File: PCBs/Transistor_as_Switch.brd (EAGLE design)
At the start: 30 x 20 mm, 7 parts, among them T1 2N3904

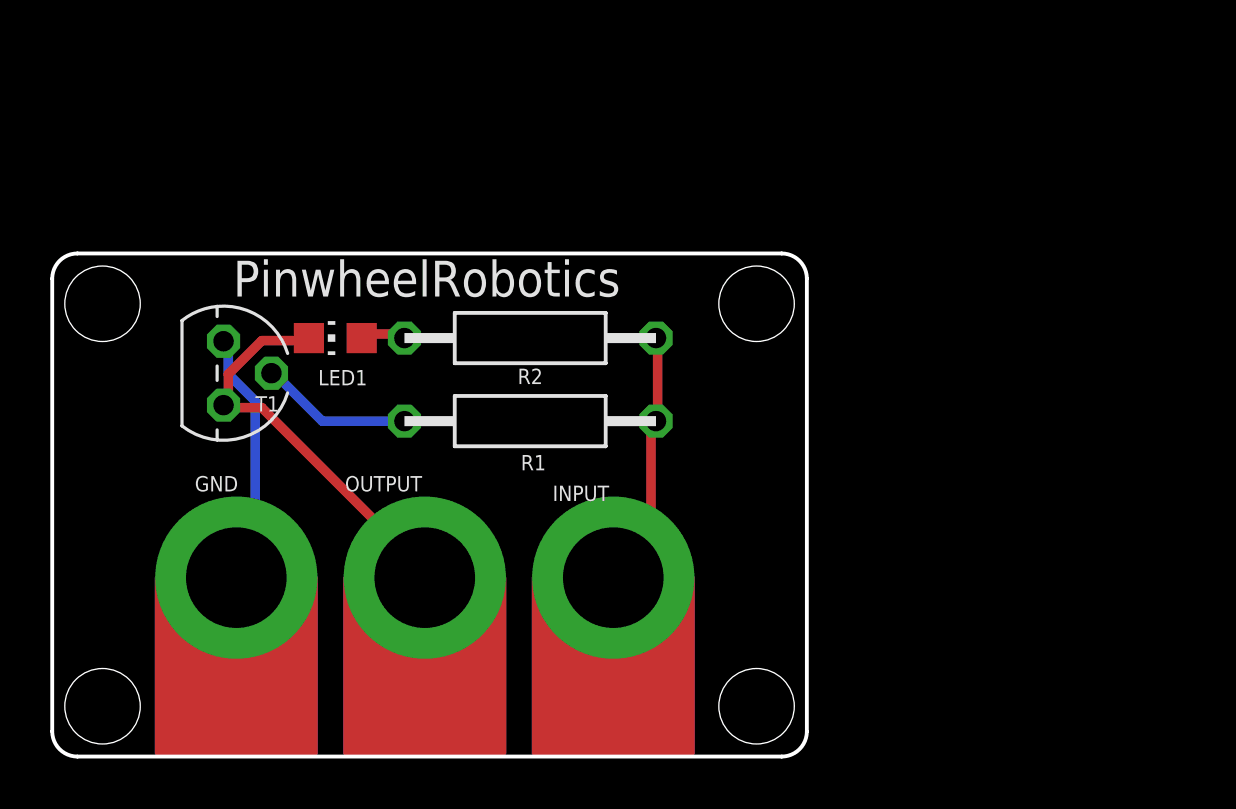
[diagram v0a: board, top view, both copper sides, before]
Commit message: Update for Dim width is 42 length is 28 for type 2 pcb
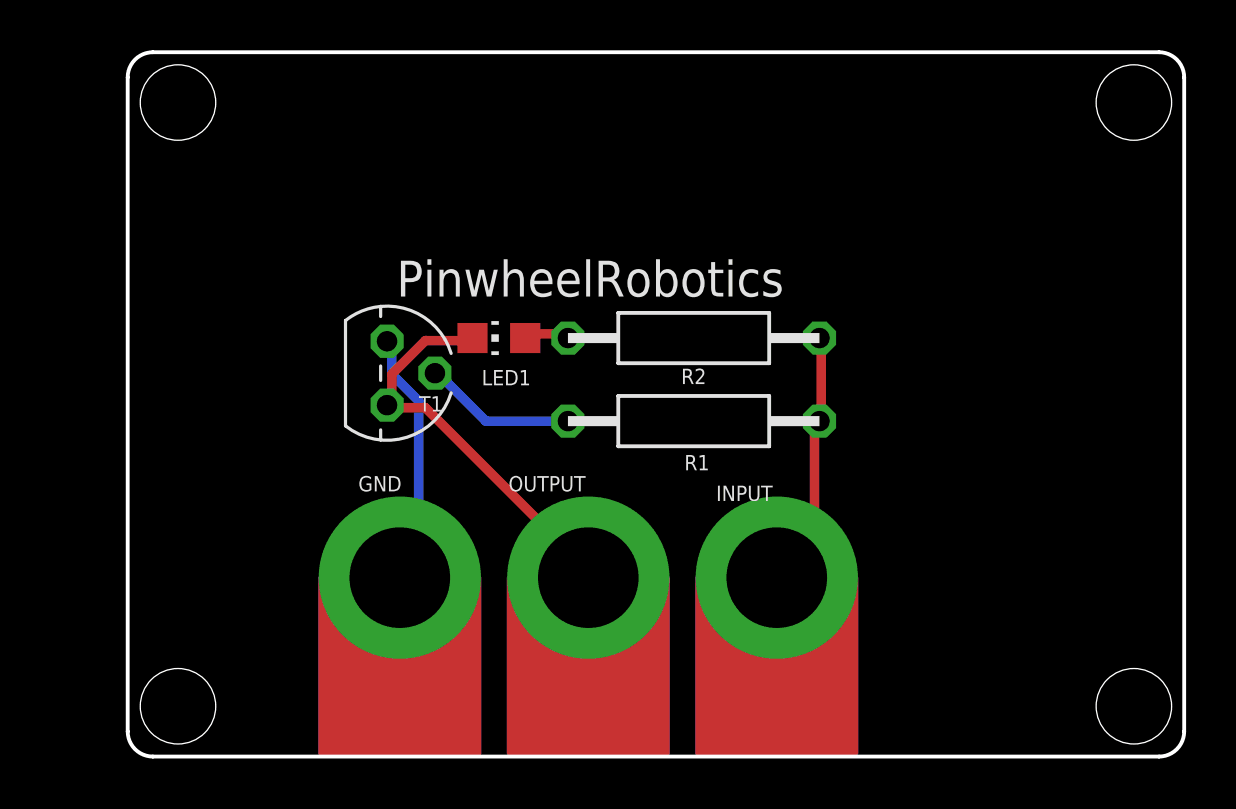
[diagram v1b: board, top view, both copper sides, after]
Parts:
- moved GND 6.50 mm to (10.8, 7.11)
- moved INPUT 6.50 mm to (25.8, 7.11)
- moved LED1 6.50 mm to (14.8, 16.6)
- moved OUTPUT 6.50 mm to (18.3, 7.11)
- moved R1 6.50 mm to (22.5, 13.3)
- moved R2 6.50 mm to (22.5, 16.6)
- moved T1 6.50 mm to (10.3, 15.2)
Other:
- board size 30 x 20 mm -> 42 x 28 mm

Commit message: Corrected hole position for some design , made transistor as switch as category 1
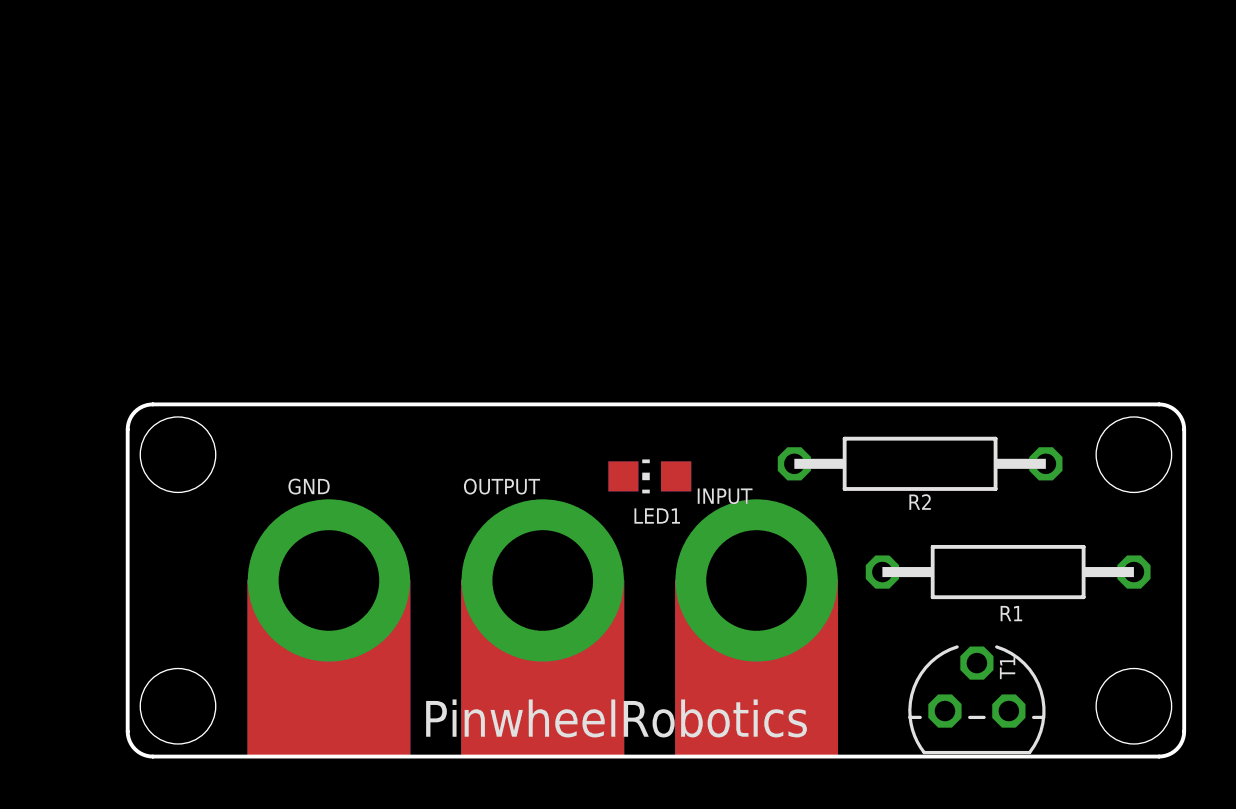
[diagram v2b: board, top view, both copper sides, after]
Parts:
- moved T1 27.0 mm to (33.8, 1.81), turned to 0 degrees
- moved R1 13.9 mm to (35.0, 7.33)
- moved R2 10.3 mm to (31.5, 11.6)
- moved LED1 8.14 mm to (20.8, 11.1)
- moved GND 2.82 mm to (8.00, 7.00)
- moved OUTPUT 1.81 mm to (16.5, 7.00)
- moved INPUT 0.81 mm to (25.0, 7.00)
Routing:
- net N$2: track 16.1 -> 0.00 mm
- net GND: track 10.3 -> 0.00 mm
- net 5V: track 10.5 -> 0.47 mm
- net N$3: track 6.06 -> 0.00 mm
- net N$1: track 1.95 -> 0.00 mm
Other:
- board size 42 x 28 mm -> 42 x 14 mm
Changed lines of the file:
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@@
 <board>
 <plain>
-<wire x1="0" y1="27" x2="0" y2="1" width="0.1524" layer="20"/>
+<wire x1="0" y1="13" x2="0" y2="1" width="0.1524" layer="20"/>
 <wire x1="0" y1="1" x2="1" y2="0" width="0.1524" layer="20" curve="90"/>
 <wire x1="1" y1="0" x2="41" y2="0" width="0.1524" layer="20"/>
 <wire x1="41" y1="0" x2="42" y2="1" width="0.1524" layer="20" curve="90"/>
-<wire x1="42" y1="1" x2="42" y2="27" width="0.1524" layer="20"/>
-<wire x1="42" y1="27" x2="41" y2="28" width="0.1524" layer="20" curve="90"/>
-<wire x1="41" y1="28" x2="1" y2="28" width="0.1524" layer="20"/>
-<wire x1="1" y1="28" x2="0" y2="27" width="0.1524" layer="20" curve="90"/>
-<hole x="2" y="26" drill="3"/>
-<hole x="40" y="26" drill="3"/>
+<wire x1="42" y1="1" x2="42" y2="13" width="0.1524" layer="20"/>
+<wire x1="42" y1="13" x2="41" y2="14" width="0.1524" layer="20" curve="90"/>
+<wire x1="41" y1="14" x2="1" y2="14" width="0.1524" layer="20"/>
+<wire x1="1" y1="14" x2="0" y2="13" width="0.1524" layer="20" curve="90"/>
+<hole x="2" y="12" drill="3"/>
+<hole x="40" y="12" drill="3"/>
 <hole x="40" y="2" drill="3"/>
 <hole x="2" y="2" drill="3"/>
-<text x="10.691" y="18.288" size="1.4224" layer="21">PinwheelRobotics</text>
+<text x="11.691" y="0.788" size="1.4224" layer="21">PinwheelRobotics</text>
 <text x="11.961" y="11.811" size="1.27" layer="22" rot="MR180">care@pinwheel.in</text>
-<dimension x1="-7" y1="0" x2="-7" y2="28" x3="-10.5" y3="14" textsize="1.778" layer="47"/>
-<dimension x1="0" y1="33" x2="42" y2="33" x3="21" y3="31" textsize="1.778" layer="47"/>
-<dimension x1="2" y1="29.5" x2="40" y2="29.5" x3="21" y3="34" textsize="1.778" layer="47"/>
-<dimension x1="45" y1="2" x2="45" y2="26" x3="47.5" y3="14" textsize="1.778" layer="47" dtype="diameter"/>
 </plain>
 <attributes>
@@
 </autorouter>
 <elements>
-<element name="GND" library="microbit" package="MICROBIT_PAD" value="MICROBIT_PAD" x="10.818" y="7.112" smashed="yes">
-<attribute name="NAME" x="9.167" y="10.541" size="0.6096" layer="21" font="vector"/>
-</element>
-<element name="INPUT" library="microbit" package="MICROBIT_PAD" value="MICROBIT_PAD" x="25.804" y="7.112" smashed="yes">
-<attribute name="NAME" x="23.391" y="10.16" size="0.6096" layer="21" font="vector"/>
-</element>
-<element name="LED1" library="led" library_urn="urn:adsk.eagle:library:259" package="CHIP-LED0805" package3d_urn="urn:adsk.eagle:package:15818/2" value="" x="14.755" y="16.637" smashed="yes" rot="R90">
-<attribute name="NAME" x="16.025" y="15.367" size="0.6096" layer="25" font="vector" rot="R180"/>
-<attribute name="POPULARITY" value="68" x="32.535" y="45.847" size="1.778" layer="27" rot="R90" display="off"/>
-<attribute name="VALUE" x="16.025" y="19.177" size="1.27" layer="27" rot="R180"/>
-</element>
-<element name="OUTPUT" library="microbit" package="MICROBIT_PAD" value="MICROBIT_PAD" x="18.311" y="7.112" smashed="yes">
-<attribute name="NAME" x="15.136" y="10.541" size="0.6096" layer="21" font="vector"/>
-</element>
-<element name="R1" library="we-rcl" package="R0207/10" value="" x="22.502" y="13.335" smashed="yes" rot="R180">
-<attribute name="NAME" x="22.629" y="11.684" size="0.6096" layer="25" font="vector" rot="R180" align="center"/>
-<attribute name="VALUE" x="22.502" y="13.335" size="0.8128" layer="27" font="vector" ratio="10" rot="R180" align="center"/>
-</element>
-<element name="R2" library="we-rcl" package="R0207/10" value="" x="22.502" y="16.637" smashed="yes">
-<attribute name="NAME" x="22.502" y="15.113" size="0.6096" layer="25" font="vector" align="center"/>
-<attribute name="VALUE" x="22.502" y="16.637" size="0.8128" layer="27" font="vector" ratio="10" align="center"/>
-</element>
-<element name="T1" library="transistor" library_urn="urn:adsk.eagle:library:402" package="TO92" package3d_urn="urn:adsk.eagle:package:28523/2" value="2N3904" x="10.31" y="15.24" smashed="yes" rot="R270">
-<attribute name="NAME" x="11.58" y="13.716" size="0.6096" layer="25" font="vector"/>
-<attribute name="POPULARITY" value="27" x="-22.71" y="-7.62" size="1.778" layer="27" rot="R270" display="off"/>
-<attribute name="VALUE" x="9.04" y="16.891" size="0.6096" layer="27" font="vector" rot="R270"/>
+<element name="GND" library="microbit" package="MICROBIT_PAD" value="MICROBIT_PAD" x="8" y="7" smashed="yes">
+<attribute name="NAME" x="6.349" y="10.429" size="0.6096" layer="21" font="vector"/>
+</element>
+<element name="INPUT" library="microbit" package="MICROBIT_PAD" value="MICROBIT_PAD" x="25" y="7" smashed="yes">
+<attribute name="NAME" x="22.587" y="10.048" size="0.6096" layer="21" font="vector"/>
+</element>
+<element name="LED1" library="led" library_urn="urn:adsk.eagle:library:259" package="CHIP-LED0805" package3d_urn="urn:adsk.eagle:package:15818/2" value="" x="20.755" y="11.137" smashed="yes" rot="R90">
+<attribute name="NAME" x="22.025" y="9.867" size="0.6096" layer="25" font="vector" rot="R180"/>
+<attribute name="POPULARITY" value="68" x="38.535" y="40.347" size="1.778" layer="27" rot="R90" display="off"/>
+<attribute name="VALUE" x="22.025" y="13.677" size="1.27" layer="27" rot="R180"/>
+</element>
+<element name="OUTPUT" library="microbit" package="MICROBIT_PAD" value="MICROBIT_PAD" x="16.5" y="7" smashed="yes">
+<attribute name="NAME" x="13.325" y="10.429" size="0.6096" layer="21" font="vector"/>
+</element>
+<element name="R1" library="we-rcl" package="R0207/10" value="" x="35.002" y="7.335" smashed="yes" rot="R180">
+<attribute name="NAME" x="35.129" y="5.684" size="0.6096" layer="25" font="vector" rot="R180" align="center"/>
+<attribute name="VALUE" x="35.002" y="7.335" size="0.8128" layer="27" font="vector" ratio="10" rot="R180" align="center"/>
+</element>
+<element name="R2" library="we-rcl" package="R0207/10" value="" x="31.502" y="11.637" smashed="yes">
+<attribute name="NAME" x="31.502" y="10.113" size="0.6096" layer="25" font="vector" align="center"/>
+<attribute name="VALUE" x="31.502" y="11.637" size="0.8128" layer="27" font="vector" ratio="10" align="center"/>
+</element>
+<element name="T1" library="transistor" library_urn="urn:adsk.eagle:library:402" package="TO92" package3d_urn="urn:adsk.eagle:package:28523/2" value="2N3904" x="33.76" y="1.81" smashed="yes">
+<attribute name="NAME" x="35.284" y="3.08" size="0.6096" layer="25" font="vector" rot="R90"/>
+<attribute name="POPULARITY" value="27" x="56.62" y="-31.21" size="1.778" layer="27" display="off"/>
+<attribute name="VALUE" x="32.109" y="0.54" size="0.6096" layer="27" font="vector"/>
 </element>
 </elements>
@@
 <contactref element="R1" pad="1"/>
 <contactref element="INPUT" pad="PAD"/>
-<wire x1="27.5693" y1="16.5354" x2="27.5693" y2="13.335" width="0.381" layer="1"/>
-<wire x1="27.5693" y1="13.335" x2="27.502" y2="13.335" width="0.381" layer="1"/>
-<wire x1="27.5693" y1="16.5354" x2="27.502" y2="16.637" width="0.381" layer="1"/>
-<wire x1="27.3026" y1="8.43429375" x2="27.3026" y2="13.335" width="0.381" layer="1"/>
-<wire x1="27.3026" y1="13.335" x2="27.502" y2="13.335" width="0.381" layer="1"/>
-<wire x1="27.3026" y1="8.43429375" x2="25.804" y2="7.112" width="0.381" layer="1"/>
+<wire x1="25" y1="7" x2="25.335" y2="7.335" width="0.381" layer="1"/>
+<wire x1="40.002" y1="7.335" x2="36.502" y2="11.637" width="0" layer="19" extent="1-1"/>
+<wire x1="25.335" y1="7.335" x2="36.502" y2="11.637" width="0" layer="19" extent="1-1"/>
 </signal>
 <signal name="N$1">
 <contactref element="R2" pad="1"/>
 <contactref element="LED1" pad="A"/>
-<wire x1="17.4347" y1="16.8021" x2="15.8345" y2="16.8021" width="0.381" layer="1"/>
-<wire x1="15.8345" y1="16.8021" x2="15.805" y2="16.637" width="0.381" layer="1"/>
-<wire x1="17.4347" y1="16.8021" x2="17.502" y2="16.637" width="0.381" layer="1"/>
+<wire x1="21.805" y1="11.137" x2="26.502" y2="11.637" width="0" layer="19" extent="1-1"/>
 </signal>
 <signal name="N$2">
@@
 <contactref element="T1" pad="1"/>
 <contactref element="OUTPUT" pad="PAD"/>
-<wire x1="11.834" y1="16.5354" x2="13.7009" y2="16.5354" width="0.381" layer="1"/>
-<wire x1="10.5005" y1="15.2019" x2="11.834" y2="16.5354" width="0.381" layer="1"/>
-<wire x1="10.5005" y1="14.1351" x2="10.5005" y2="15.2019" width="0.381" layer="1"/>
-<wire x1="13.7009" y1="16.5354" x2="13.705" y2="16.637" width="0.381" layer="1"/>
-<wire x1="10.5005" y1="14.1351" x2="10.31" y2="13.97" width="0.381" layer="1"/>
-<wire x1="11.834" y1="13.8684" x2="10.5005" y2="13.8684" width="0.381" layer="1"/>
-<wire x1="18.194584375" y1="7.507815625" x2="11.834" y2="13.8684" width="0.381" layer="1"/>
-<wire x1="10.5005" y1="13.8684" x2="10.31" y2="13.97" width="0.381" layer="1"/>
-<wire x1="18.194584375" y1="7.507815625" x2="18.311" y2="7.112" width="0.381" layer="1"/>
+<wire x1="19.705" y1="11.137" x2="35.03" y2="1.81" width="0" layer="19" extent="1-1"/>
+<wire x1="16.5" y1="7" x2="19.705" y2="11.137" width="0" layer="19" extent="1-1"/>
 </signal>
 <signal name="GND">
 <contactref element="T1" pad="3"/>
 <contactref element="GND" pad="PAD"/>
-<wire x1="10.5005" y1="15.2019" x2="10.5005" y2="16.2687" width="0.381" layer="16"/>
-<wire x1="11.5673" y1="14.1351" x2="10.5005" y2="15.2019" width="0.381" layer="16"/>
-<wire x1="11.5673" y1="7.7343" x2="11.5673" y2="14.1351" width="0.381" layer="16"/>
-<wire x1="11.0339" y1="7.2009" x2="11.5673" y2="7.7343" width="0.381" layer="16"/>
-<wire x1="10.5005" y1="16.2687" x2="10.31" y2="16.51" width="0.381" layer="16"/>
-<wire x1="11.0339" y1="7.2009" x2="10.818" y2="7.112" width="0.381" layer="16"/>
+<wire x1="8" y1="7" x2="32.49" y2="1.81" width="0" layer="19" extent="1-1"/>
 </signal>
 <signal name="N$3">
 <contactref element="R1" pad="2"/>
 <contactref element="T1" pad="2"/>
-<wire x1="14.2343" y1="13.335" x2="17.502" y2="13.335" width="0.381" layer="16"/>
-<wire x1="12.3674" y1="15.2019" x2="14.2343" y2="13.335" width="0.381" layer="16"/>
-<wire x1="12.3674" y1="15.2019" x2="12.215" y2="15.24" width="0.381" layer="16"/>
+<wire x1="30.002" y1="7.335" x2="33.76" y2="3.715" width="0" layer="19" extent="1-1"/>
 </signal>
 </signals>
